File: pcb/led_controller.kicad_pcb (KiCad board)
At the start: 2 copper layers, 73 parts, among them IC1 ATTINY2313A-S, P1 POSITIVE_OUT_1, P10 NEGATIVE_OUT_1, P11 NEGATIVE_OUT_2, P12 NEGATIVE_OUT_2, P13 NEGATIVE_OUT_2, P14 ISP, P15 +12v IN, P16 GND IN, P2 POSITIVE_OUT_2, P3 POSITIVE_OUT_3, P4 POSITIVE_OUT_4, P5 WIFI, P6 POSITIVE_OUT_5, P7 POSITIVE_OUT_6, P8 NEGATIVE_OUT_1, P9 NEGATIVE_OUT_1, Q1 MOSFET_P, Q10 MOSFET_N, Q2 MOSFET_P, Q3 MOSFET_P, Q4 MOSFET_P, Q5 MOSFET_P, Q6 MOSFET_P, Q7 BS170, Q8 BS170, Q9 MOSFET_N, SW1 B1, SW2 B2, U1 TC4426A, U2 TC4426A, U3 TC4426A, U4 TC4427A, U5 MCP1700, U6 MC34063, X1 20MHz

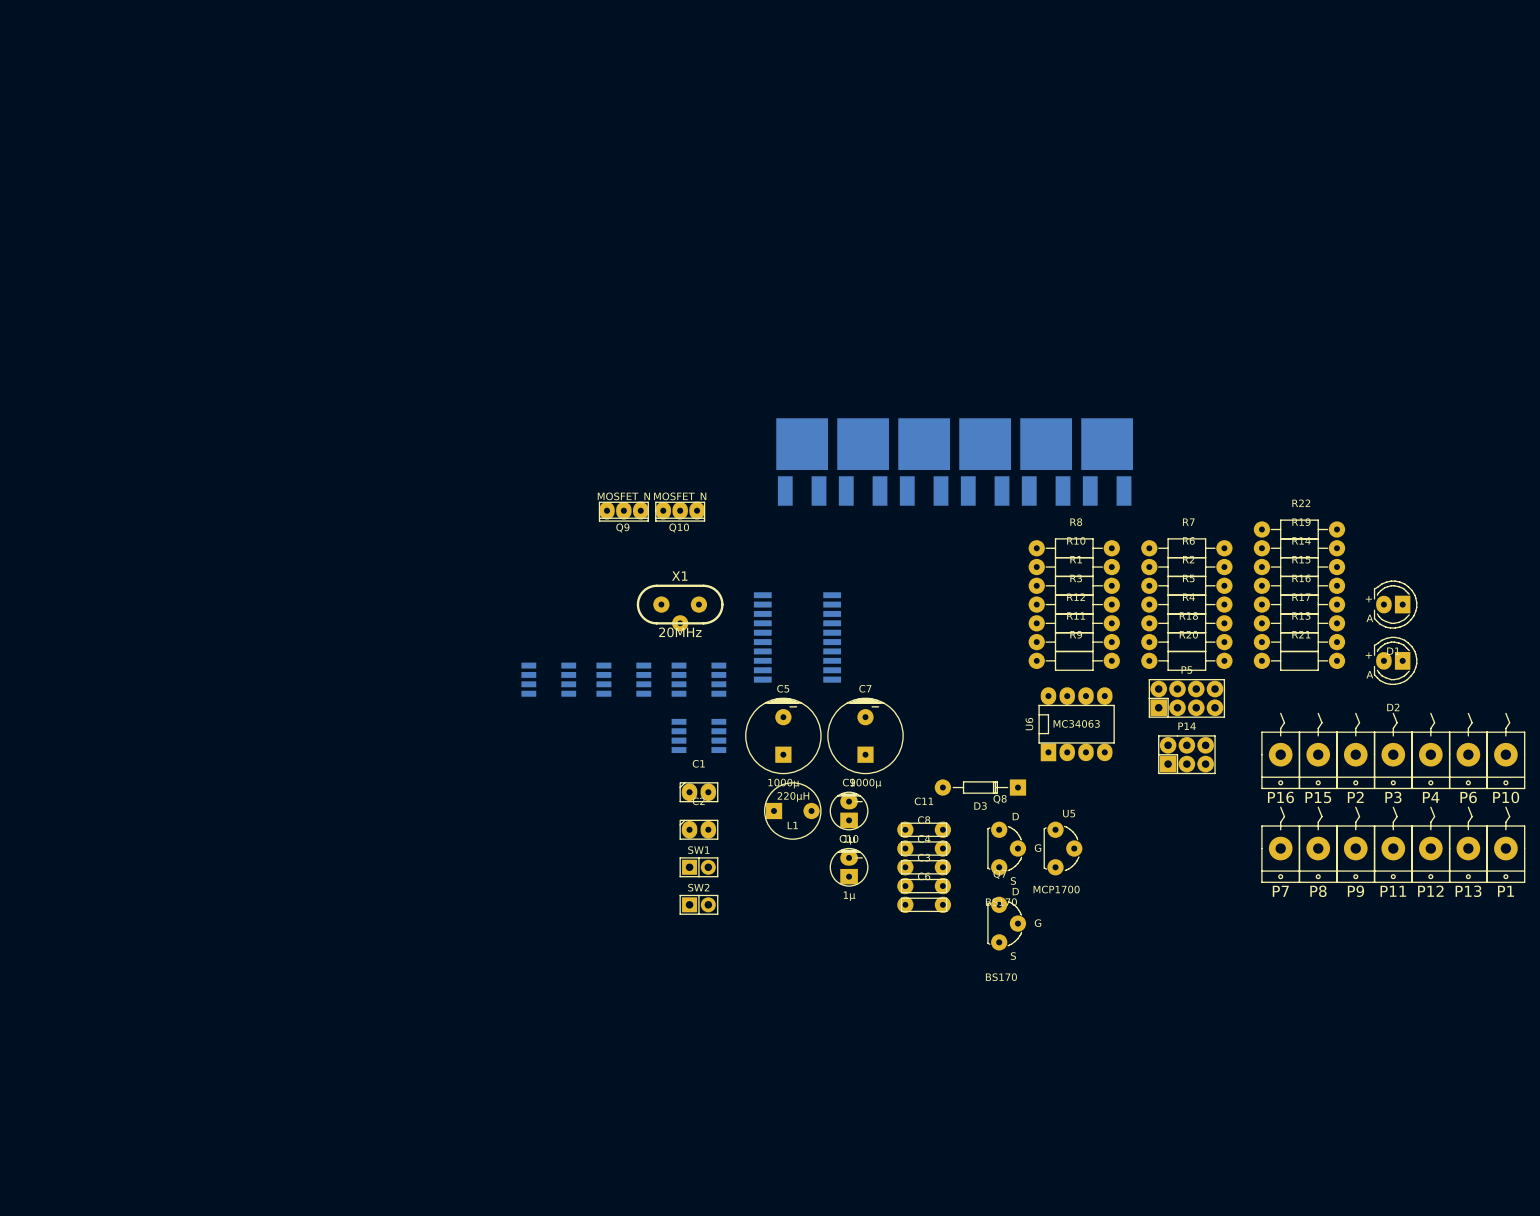
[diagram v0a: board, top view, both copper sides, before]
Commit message: 5v step-down
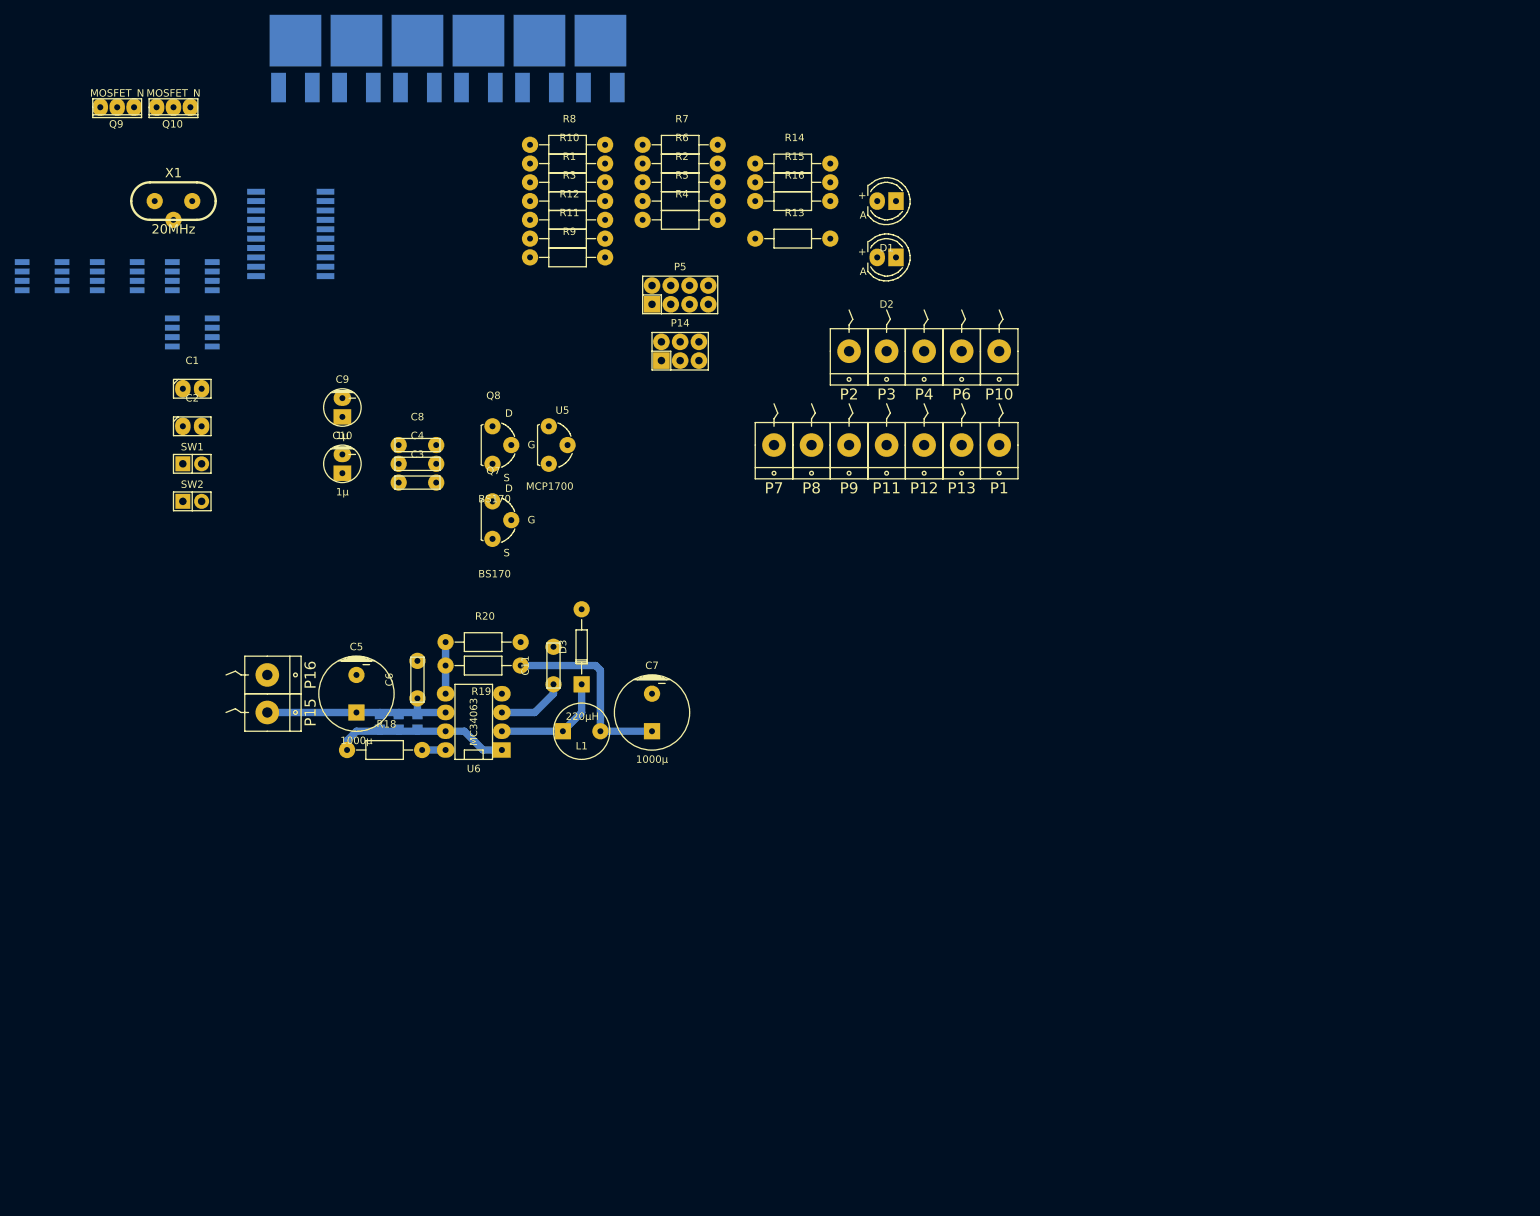
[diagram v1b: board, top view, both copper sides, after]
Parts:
- R17, R21, R22: footprint Resistors_ThroughHole:Resistor_Horizontal_RM10mm -> Resistors_SMD:R_0805; moved to B.Cu
- moved P15 142.4 mm to (55.9, 111.1), turned to 90 degrees
- moved P16 137.6 mm to (55.9, 106.0), turned to 90 degrees
- moved R21 124.7 mm to (71.1, 112.4), turned to 270 degrees
- moved R22 124.7 mm to (73.7, 112.4), turned to 270 degrees
- moved R17 120.1 mm to (76.2, 112.4), turned to 270 degrees
- moved R19 111.6 mm to (85.1, 104.8), turned to 180 degrees
- moved R18 109.6 mm to (71.8, 116.2)
- moved R20 95.3 mm to (85.1, 101.6)
- moved C10 87.7 mm to (66.0, 77.5)
- moved C4 87.7 mm to (76.2, 77.5)
- moved D1 87.7 mm to (139.7, 41.9)
- moved D2 87.7 mm to (139.7, 49.5)
- moved IC1 87.7 mm to (59.1, 46.4)
- moved P10 87.7 mm to (154.9, 62.2)
- moved P3 87.7 mm to (139.7, 62.2)
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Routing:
- net VDD: track 0.00 -> 27.3 mm
- net +5V: track 0.00 -> 26.3 mm
- net Net-(R17-Pad2): track 0.00 -> 24.8 mm
- net Net-(D3-Pad2): track 0.00 -> 15.7 mm
- net Net-(C11-Pad1): track 0.00 -> 9.31 mm
- net Net-(R19-Pad2): track 0.00 -> 6.98 mm
- net Net-(R18-Pad2): track 0.00 -> 3.18 mm

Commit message: arrange mosfets
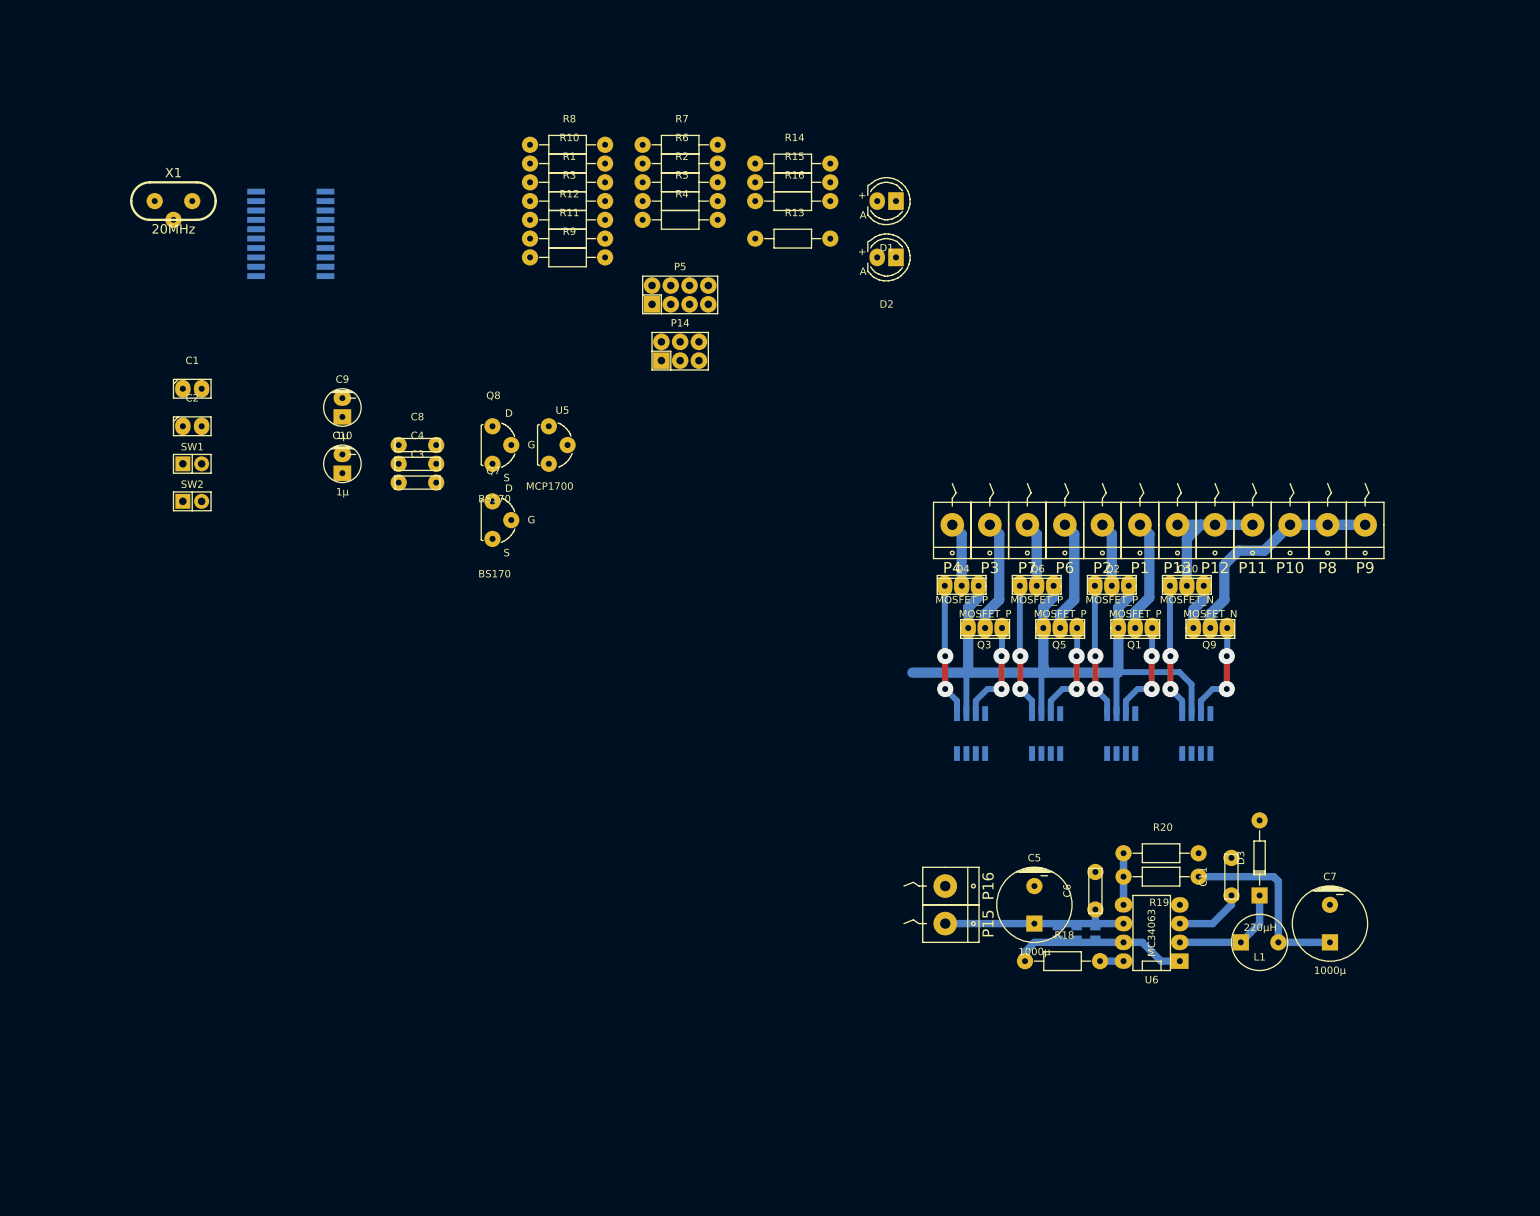
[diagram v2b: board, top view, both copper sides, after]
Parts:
- Q1, Q2, Q3, Q4, Q5, Q6: footprint SMD_Packages:DPAK-3_GDS -> SMD_Packages:IPAK-3_GDS; moved to F.Cu
- moved U4 168.0 mm to (181.6, 114.0), turned to 90 degrees
- moved Q9 163.9 mm to (183.5, 99.7)
- moved Q10 151.7 mm to (180.3, 94.0), turned to 180 degrees
- moved U1 137.0 mm to (171.4, 114.0), turned to 90 degrees
- moved U2 131.1 mm to (151.1, 114.0), turned to 90 degrees
- moved U3 131.1 mm to (161.3, 114.0), turned to 90 degrees
- moved Q5 121.6 mm to (163.2, 99.7), turned to 0 degrees
- moved Q4 114.1 mm to (149.9, 94.0)
- moved Q2 110.6 mm to (170.2, 94.0)
- moved Q1 110.5 mm to (173.4, 99.7), turned to 0 degrees
- moved Q3 107.8 mm to (153.0, 99.7), turned to 0 degrees
- moved D3 96.1 mm to (190.2, 130.8)
- moved L1 96.1 mm to (190.2, 142.2)
- moved R17 96.1 mm to (168.0, 141.0)
- moved C11 96.1 mm to (186.4, 133.3)
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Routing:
- net VDD: track 27.3 -> 125.7 mm
- net Net-(P10-Pad1): track 0.00 -> 31.6 mm
- net Net-(P11-Pad1): track 0.00 -> 19.2 mm
- net Net-(Q10-PadG): track 0.00 -> 18.0 mm, vias 0 -> 2
- net Net-(Q6-PadG): track 0.00 -> 18.0 mm, vias 0 -> 2
- net Net-(Q4-PadG): track 0.00 -> 18.0 mm, vias 0 -> 2
- net Net-(Q2-PadG): track 0.00 -> 18.0 mm, vias 0 -> 2
- net Net-(P3-Pad1): track 0.00 -> 15.3 mm
- net Net-(P6-Pad1): track 0.00 -> 15.3 mm
- net Net-(P1-Pad1): track 0.00 -> 15.3 mm
- net Net-(Q3-PadG): track 0.00 -> 14.2 mm, vias 0 -> 2
- net Net-(Q9-PadG): track 0.00 -> 14.2 mm, vias 0 -> 2
- net Net-(Q5-PadG): track 0.00 -> 14.2 mm, vias 0 -> 2
- net Net-(Q1-PadG): track 0.00 -> 14.2 mm, vias 0 -> 2
- net Net-(P7-Pad1): track 0.00 -> 8.78 mm
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
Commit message: draw symbol and footprint for the esp8266 module
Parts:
- P5: value WIFI -> ESP8266; footprint Pin_Headers:Pin_Header_Straight_2x04 -> esp8266:ESP8266_Module
- moved IC1 131.0 mm to (161.3, 128.3), turned to 270 degrees
- moved C11 102.9 mm to (84.8, 149.5)
- moved C6 102.9 mm to (66.4, 151.4)
- moved C7 102.9 mm to (98.1, 155.9)
- moved D3 102.9 mm to (88.6, 147.0)
- moved L1 102.9 mm to (88.6, 158.4)
- moved R17 102.9 mm to (66.4, 157.2)
- moved C5 102.9 mm to (58.1, 153.4)
- moved P15 102.9 mm to (46.0, 155.9)
- moved P16 102.9 mm to (46.0, 150.8)
- moved R18 102.9 mm to (61.9, 161.0)
- moved R19 102.9 mm to (75.2, 149.5)
- moved R20 102.9 mm to (75.2, 146.4)
- moved R21 102.9 mm to (61.3, 157.2)
- moved R22 102.9 mm to (63.8, 157.2)
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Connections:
- IC1 pad 11: /P5 -> /P2
- IC1 pad 12: /P6 -> /P1
- IC1 pad 6: /P1 -> /P4
- IC1 pad 7: /P2 -> /P3
- IC1 pad 8: /P3 -> /P6
- IC1 pad 9: /P4 -> /P5
- R10 pad 1: Net-(P5-Pad5) -> +3V3
- R10 pad 2: +3V3 -> Net-(P5-Pad5)
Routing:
- net GND: track 6.29 -> 63.1 mm

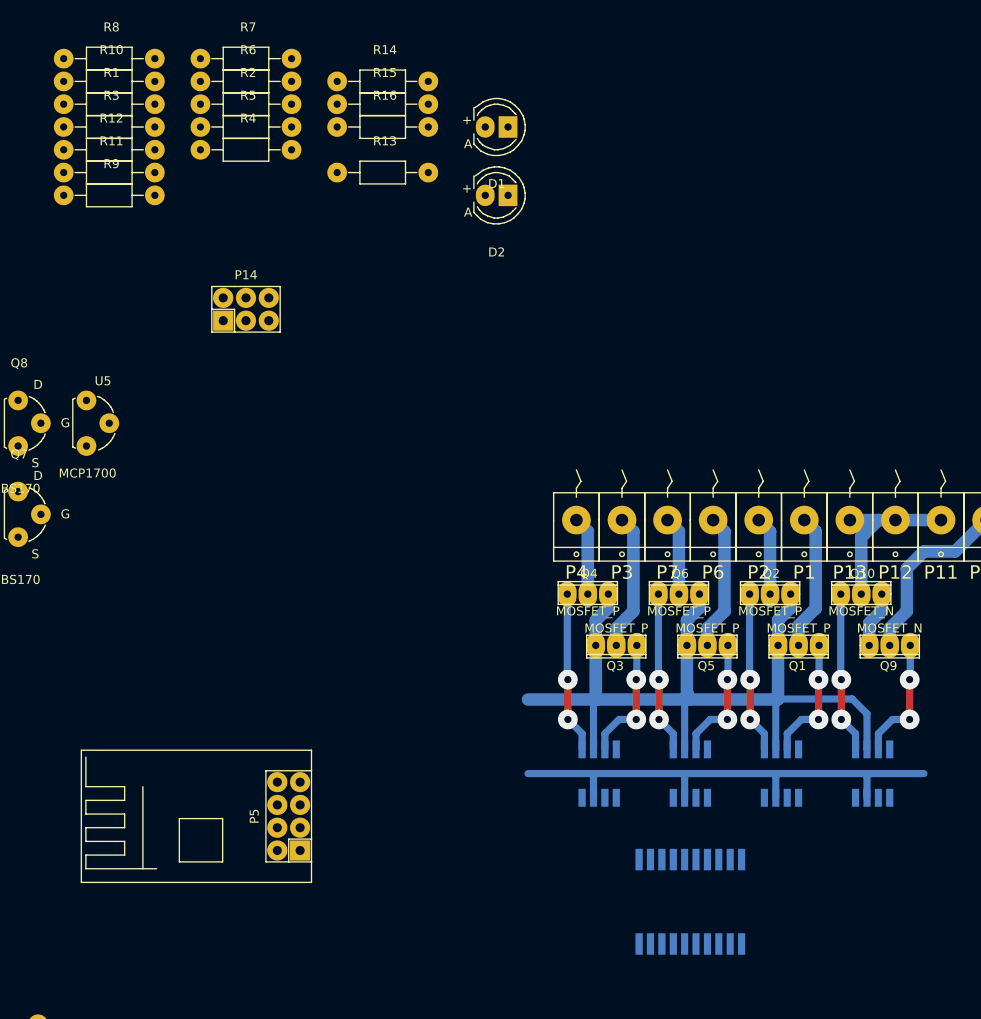
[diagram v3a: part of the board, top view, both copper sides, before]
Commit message: connect drivers to the mcu
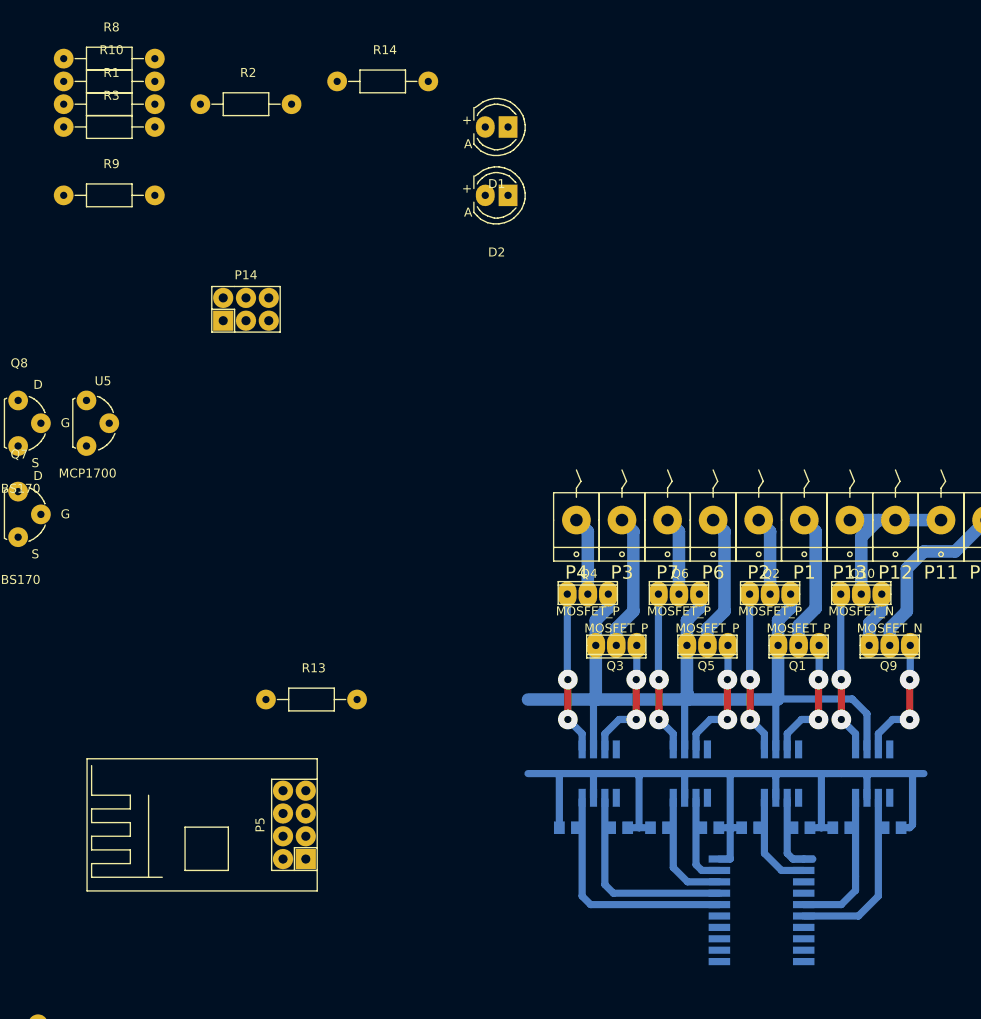
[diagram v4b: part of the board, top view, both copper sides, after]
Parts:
- R11, R12, R15, R16, R4, R5, R6, R7: footprint Resistors_ThroughHole:Resistor_Horizontal_RM10mm -> Resistors_SMD:R_0805; moved to B.Cu
- moved R11 99.1 mm to (163.5, 120.0)
- moved R15 98.7 mm to (183.8, 120.0)
- moved R4 97.7 mm to (173.7, 120.0)
- moved R12 97.3 mm to (157.8, 120.0), turned to 180 degrees
- moved R5 96.2 mm to (168.0, 120.0), turned to 180 degrees
- moved R16 93.3 mm to (178.1, 120.0), turned to 180 degrees
- moved R6 93.0 mm to (153.4, 120.0)
- moved R7 92.9 mm to (147.6, 120.0), turned to 180 degrees
- moved R13 59.3 mm to (119.1, 105.7)
- moved IC1 7.99 mm to (169.2, 129.2), turned to 0 degrees
- moved P5 1.14 mm to (117.2, 119.7)
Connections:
- IC1 pad 11: /P2 -> /P1
- IC1 pad 12: /P1 -> /P2
- IC1 pad 15: /N1 -> /N2
- IC1 pad 16: /N2 -> /N1
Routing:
- net GND: track 63.1 -> 109.3 mm
- net /P4: track 0.00 -> 26.5 mm
- net /P3: track 0.00 -> 22.7 mm
- net /N1: track 0.00 -> 20.0 mm
- net /N2: track 0.00 -> 16.6 mm
- net /P6: track 0.00 -> 13.4 mm
- net /P2: track 0.00 -> 11.2 mm
- net /P5: track 0.00 -> 10.2 mm
- net /P1: track 0.00 -> 9.15 mm

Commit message: everything except power supply
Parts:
- removed R10: 10k, Resistors_ThroughHole:Resistor_Horizontal_RM10mm
- P14: footprint Pin_Headers:Pin_Header_Straight_2x03 -> Pin_Headers:Pin_Header_Straight_1x06
- R13, R14, R8, R9: footprint Resistors_ThroughHole:Resistor_Horizontal_RM10mm -> Resistors_SMD:R_0805; moved to B.Cu
- moved SW1 150.2 mm to (184.8, 134.3)
- moved SW2 147.5 mm to (184.8, 131.8)
- moved X1 142.4 mm to (153.4, 132.1)
- moved R1 136.2 mm to (183.2, 144.5), turned to 90 degrees
- moved R8 134.1 mm to (160.0, 152.4), turned to 90 degrees
- moved C1 130.8 mm to (155.9, 137.8), turned to 180 degrees
- moved C2 123.8 mm to (150.8, 137.8)
- moved R3 121.3 mm to (183.8, 126.0), turned to 180 degrees
- moved C8 116.9 mm to (173.7, 139.4), turned to 180 degrees
- moved R2 110.5 mm to (183.8, 123.2), turned to 180 degrees
- moved R9 106.5 mm to (144.1, 144.8)
- moved R14 106.4 mm to (145.4, 141.6)
- moved P14 101.6 mm to (179.4, 138.1), turned to 270 degrees
- moved Q8 95.8 mm to (149.9, 146.7)
- moved Q7 92.9 mm to (155.9, 146.7)
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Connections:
- P14 pad 1: /MISO -> /MOSI
- P14 pad 2: +5V -> /MISO
- P14 pad 4: /MOSI -> +5V
- P14 pad 5: /RESET -> GND
- P14 pad 6: GND -> /RESET
- P5 pad 5: Net-(P5-Pad5) -> +3V3
- X1 pad 1: Net-(C1-Pad1) -> Net-(C2-Pad1)
- X1 pad 2: Net-(C2-Pad1) -> Net-(C1-Pad1)
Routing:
- net GND: track 109.3 -> 171.4 mm
- net /RX_WIFI: track 0.00 -> 38.3 mm
- net +3V3: track 0.00 -> 36.4 mm
- net /RESET: track 0.00 -> 33.6 mm, vias 0 -> 2
- net /TX_AVR: track 0.00 -> 23.3 mm
- net Net-(C2-Pad1): track 0.00 -> 20.9 mm
- net Net-(D2-Pad1): track 0.00 -> 18.1 mm
- net /RX_AVR: track 0.00 -> 17.4 mm
- net Net-(C1-Pad1): track 0.00 -> 14.7 mm
- net +5V: track 26.3 -> 39.6 mm
- net /TX_WIFI: track 0.00 -> 10.8 mm
- net /MISO: track 0.00 -> 10.4 mm
- net /MOSI: track 0.00 -> 9.85 mm
- net /SCK: track 0.00 -> 6.78 mm
- net Net-(IC1-Pad13): track 0.00 -> 6.75 mm
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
